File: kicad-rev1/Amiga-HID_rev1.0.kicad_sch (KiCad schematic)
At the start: 0 parts

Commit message: One Top-Level Schematic
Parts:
- added C1: 10uF, Capacitor_SMD:C_0805_2012Metric, symbol Device:C
- added C10, C9: 4.7u, Capacitor_SMD:C_0402_1005Metric, symbol Device:C
- added C11, C12, C13, C14, C15, C16, C17, C18, C2, C8: 100n, Capacitor_SMD:C_0402_1005Metric, symbol Device:C
- added C19: 10u, Capacitor_SMD:C_0805_2012Metric, symbol Device:C
- added C2, C21, C23, C4: 100nF, Capacitor_SMD:C_0402_1005Metric, symbol Device:C
- added C3: 22uF, Capacitor_SMD:C_0805_2012Metric, symbol Device:C
- added C3, C4: 15p, Capacitor_SMD:C_0402_1005Metric, symbol Device:C
- added C6, C7: 4.7u, Amiga-HID_rev1.0:C_0402_1005Metric_small_pads, symbol Device:C
- added D1, D2, D3: PMEG2010AEH, Diode_SMD:D_SOD-323, symbol Device:D_Schottky
- added F1: 500mA, Fuse:Fuse_1206_3216Metric, symbol Device:Polyfuse
- added J1: USB-A Host, Connector_USB:USB_A_Stewart_SS-52100-001_Horizontal, symbol Connector:USB_A
- added J2: JST-XH-5A, Connector_JST:JST_XH_B5B-XH-A_1x05_P2.50mm_Vertical, symbol Connector_Generic:Conn_01x05
- added J3: OLED I2C, Connector_PinHeader_2.54mm:PinHeader_1x04_P2.54mm_Vertical, symbol Connector_Generic:Conn_01x04
- added J4: Reserve 3V3+GP+GND+VSYS, Connector_PinHeader_2.54mm:PinHeader_1x05_P2.54mm_Vertical, symbol Connector_Generic:Conn_01x05
- added J5: JST-SH-3 SWD, Connector_JST:JST_SH_SM03B-SRSS-TB_1x03-1MP_P1.00mm_Horizontal, symbol Connector_Generic:Conn_01x03
- added J6: JST-SH-3 UART, Connector_JST:JST_SH_SM03B-SRSS-TB_1x03-1MP_P1.00mm_Horizontal, symbol Connector_Generic:Conn_01x03
- added L1: 3.3u, Amiga-HID_rev1.0:L_pol_2016, symbol Device:L
- added LED1: Status_Green, LED_SMD:LED_0603_1608Metric, symbol Device:LED
- added LED2: Activity_Yellow, LED_SMD:LED_0603_1608Metric, symbol Device:LED
- added R1, R9: DNF, Resistor_SMD:R_0402_1005Metric, symbol Device:R
- added R1, R2: 1k, Resistor_SMD:R_0603_1608Metric, symbol Device:R
- added R10: 0, Resistor_SMD:R_0402_1005Metric, symbol Device:R
- added R2, R4, R6: 1k, Resistor_SMD:R_0402_1005Metric, symbol Device:R
- added R5: 33, Resistor_SMD:R_0402_1005Metric, symbol Device:R
- added R7, R8: 27, Resistor_SMD:R_0402_1005Metric, symbol Device:R
- added SJ1: OLED_VCC_SEL, Jumper:SolderJumper-3_P1.3mm_Open_TrianglePad1.0x1.5mm, symbol Jumper:SolderJumper_3_Bridged12
- added SW1, SW2: SW_Push, Button_Switch_SMD:SW_Push_1P1T_NO_Vertical_Wuerth_434133025816, symbol Switch:SW_Push
- added U1: RP2350_60QFN, Amiga-HID_rev1.0:RP2350-QFN-60-1EP_7x7_P0.4mm_EP3.4x3.4mm_ThermalVias, symbol MCU_RaspberryPi_RP2350:RP2350_60QFN
- added U1: USBLC6-2SC6, Package_TO_SOT_SMD:SOT-23-6, symbol Power_Protection:USBLC6-2SC6
- added U2: AMS1117-3.3, Package_TO_SOT_SMD:SOT-223-3_TabPin2, symbol Regulator_Linear:AMS1117-3.3
- added U3: W25Q128JVS, Package_SO:SOIC-8_5.23x5.23mm_P1.27mm, symbol Memory_Flash:W25Q128JVS
- added U5: TXS0102DCUR, Package_SO:VSSOP-8_2.4x2.0mm_P0.5mm, symbol Custom:TXS0102
- added Y1: ABM8-272-T3, Crystal:Crystal_SMD_3225-4Pin_3.2x2.5mm, symbol Device:Crystal_GND24
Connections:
- new net: R7.2, U1.52 (USB_DP)
- new net: R8.2, U1.51 (USB_DM)
- new net: J3.2 (Pin_2), SJ1.1 (A)
- new net: R4.1, SW2.1
- new net: LED1.1 (K), R1.1
- new net: LED2.1 (K), R2.2
- new net: C4.1, R2.2, Y1.3
- new net: D3.1 (K), F1.1
- new net +1V1: C10.1, C11.1, C7.1, C8.1, L1.1, U1.23 (DVDD), U1.39 (DVDD), U1.50 (VREG_FB), U1.6 (DVDD)
- new net +3V3: C12.1, C13.1, C14.1, C15.1, C16.1, C17.1, C18.1, C19.1, C2.1, C21.2, C3.1, C4.1, C6.1, J4.3 (Pin_3), R1.1, R5.1, SJ1.2 (C), U1.1 (IOVDD), U1.11 (IOVDD), U1.20 (IOVDD), U1.30 (IOVDD), U1.38 (IOVDD), U1.44 (ADC_AVDD), U1.45 (IOVDD), U1.49 (VREG_VIN), U1.53 (USB_OTP_VDD), U1.54 (QSPI_IOVDD), U2.2 (VO), U3.8 (VCC), U5.1 (VCCA), U5.5 (OE)
- new net +5V_AMIGA: D2.2 (A), J2.4 (Pin_4)
- new net FLASH_SS: R1.2, R10.2, R9.2, U3.1 (~{CS})
- new net GND: C1.2, C10.2, C11.2, C12.2, C13.2, C14.2, C15.2, C16.2, C17.2, C18.2, C19.2, C2.2, C2.2, C21.1, C23.1, C3.2, C3.2, C4.2, C4.2, C6.2, C7.2, C8.2, C9.2, J1.4 (GND), J1.5 (Shield), J2.5 (Pin_5), J3.1 (Pin_1), J4.2 (Pin_2), J5.2 (Pin_2), J6.2 (Pin_2), LED1.2 (A), LED2.2 (A), R4.2, SW1.1, U1.2 (GND), U1.47 (VREG_PGND), U1.61 (GND), U2.1 (GND), U3.4 (GND), U5.4 (GND), Y1.2, Y1.4
- new net GPIO10: U1.14 (GPIO10)
- new net GPIO11: U1.15 (GPIO11)
- new net GPIO12: U1.16 (GPIO12)
- new net GPIO13: U1.17 (GPIO13)
- new net GPIO14: U1.18 (GPIO14)
- new net GPIO15: U1.19 (GPIO15)
- new net GPIO17: U1.28 (GPIO17)
- new net GPIO18: U1.29 (GPIO18)
- new net GPIO19: U1.31 (GPIO19)
- new net GPIO20: U1.32 (GPIO20)
- new net GPIO21: U1.33 (GPIO21)
- new net GPIO22: U1.34 (GPIO22)
- new net GPIO23: U1.35 (GPIO23)
- new net GPIO24: U1.36 (GPIO24)
- new net GPIO26_ADC0: U1.40 (GPIO26_ADC0)
- new net GPIO27_ADC1: U1.41 (GPIO27_ADC1)
- new net GPIO28_ADC2: U1.42 (GPIO28_ADC2)
- new net GPIO29_ADC3: U1.43 (GPIO29_ADC3)
- new net GPIO4: U1.7 (GPIO4)
- new net GPIO9: U1.13 (GPIO9)
- new net GP_RES1: J4.4 (Pin_4), U1.10 (GPIO7)
- new net GP_RES2: J4.5 (Pin_5), U1.12 (GPIO8)
- new net I2C1_SCL: J3.3 (Pin_3), U1.5 (GPIO3)
- new net I2C1_SDA: J3.4 (Pin_4), U1.4 (GPIO2)
- new net KB_CLOCK_3V3: U1.9 (GPIO6), U5.3 (A2)
- new net KB_CLOCK_5V: J2.1 (Pin_1), U5.6 (B2)
- new net KB_DATA_3V3: U1.8 (GPIO5), U5.2 (A1)
- new net KB_DATA_5V: J2.3 (Pin_3), U5.7 (B1)
- new net LED1: R1.2, U1.37 (GPIO25)
- new net LED2: R2.1, U1.27 (GPIO16)
- new net QSPI_SCLK: U1.56 (QSPI_SCLK), U3.6 (CLK)
- new net QSPI_SD0: U1.57 (QSPI_SD0), U3.5 (DI(IO0))
- new net QSPI_SD1: U1.59 (QSPI_SD1), U3.2 (DO(IO1))
- new net QSPI_SD2: U1.58 (QSPI_SD2), U3.3 (IO2)
- new net QSPI_SD3: U1.55 (QSPI_SD3), U3.7 (IO3)
- new net QSPI_SS: R10.1, R6.1, U1.60 (QSPI_SS)
- new net RUN: SW2.2, U1.26 (RUN)
- new net SWCLK: J5.1 (Pin_1), U1.24 (SWCLK)
- new net SWDIO: J5.3 (Pin_3), U1.25 (SWD)
- new net UART_RX: J6.3 (Pin_3), U1.3 (GPIO1)
- new net UART_TX: J6.1 (Pin_1), R9.1, U1.2 (GPIO0)
- new net USB_D+: J1.3 (D+), U1.1 (I/O1)
- new net USB_D-: J1.2 (D-), U1.3 (I/O2)
- new net USB_DM: R8.1, U1.4 (I/O2)
- new net USB_DP: R7.1, U1.6 (I/O1)
- new net VBUS: C23.2, D1.2 (A), F1.2, J1.1 (VBUS), U1.5 (VBUS), U5.8 (VCCB)
- new net VREG_AVDD: C9.1, R5.2, U1.46 (VREG_AVDD)
- new net VREG_LX: L1.2, U1.48 (VREG_LX)
- new net VSYS: C1.1, C2.1, D1.1 (K), D2.1 (K), D3.2 (A), J4.1 (Pin_1), SJ1.3 (B), U2.3 (VI)
- new net XIN: C3.1, U1.21 (XIN), Y1.1
- new net XOUT: R2.1, U1.22 (XOUT)
- new net ~{USB_BOOT}: R6.2, SW1.2
- no-connect marks 0 -> 21
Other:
- removed sheet MCU
- removed sheet Power
- note added: "12MHz Crystal"
- note added: "Debug-Pads Bereich A (1.0mm Pitch) - Pi Debug Probe"
- note added: "Debug-Pads Bereich B (2.54mm Pitch) - OLED + Reserve"
- note added: "Flash"
- note added: "Level Shifter TXS0102 -- 3V3 (RP2350) <-> 5V (Amiga)"
- note added: "Make sure R7 and R8 are close to RP2350"
- note added: "Signale vom/zum MCU-Sheet:"
- note added: "Status & Activity LEDs"
- note added: "USB-A Buchse (Host: Tastatur / Service: PC fuer Flash)"
- note added: "VSYS rail = 4.8 V worst-case\nKeyboard sees ~4.55 V via D3+F1 (within USB spec)"
- note removed: "Amiga-HID rev1.0 - top level. Iteration 1: Power section only. Further sheets (mcu, usb, level_shifter, connectors_debug) to be added."
- title: Amiga-HID rev1.0 - Top Level -> Amiga-HID rev1.0

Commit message: Footprints sind vollständig
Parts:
- added J7: Conn_01x06_Pin, Connector_PinHeader_1.27mm:PinHeader_1x06_P1.27mm_Vertical, symbol Connector:Conn_01x06_Pin
- C8: renamed from C6; footprint Amiga-HID_rev1.0:C_0402_1005Metric_small_pads -> Capacitor_SMD:C_0402_1005Metric
- C9: renamed from C7; footprint Amiga-HID_rev1.0:C_0402_1005Metric_small_pads -> Capacitor_SMD:C_0402_1005Metric
- L1: value 3.3u -> 2.2u; Alternate (none) -> 3.3uH: Sunlord MWSA201610H3R3MT (LCSC C408237) - same footp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; LCSC (none) -> C408232; MPN (none) -> MWSA201610H2R2MT; Manufacturer (none) -> Sunlord
- SJ1: footprint Jumper:SolderJumper-3_P1.3mm_Open_TrianglePad1.0x1.5mm -> Jumper:SolderJumper-3_P1.3mm_Open_Pad1.0x1.5mm
- U5: footprint Package_SO:VSSOP-8_2.4x2.0mm_P0.5mm -> Package_SO:VSSOP-8_2.3x2mm_P0.5mm
- Y1: value ABM8-272-T3 -> 12MHz_3225_8pF
- renumbered C8 to C10, C9 to C11, C10 to C12, C11 to C13, C19 to C14, C12 to C15, C13 to C16, C14 to C17, C15 to C18, C16 to C19, C17 to C20, C18 to C22, C3 to C5, C4 to C6, C2 to C7, R7 to R10, R8 to R11, R9 to R3, R10 to R4, R1 to R5, R2 to R6, R4 to R7, R5 to R8, R6 to R9, U1 to U4
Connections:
- net GND: now also J7.2 (Pin_2), J7.5 (Pin_5)
- net SWCLK: now also J7.1 (Pin_1)
- net SWDIO: now also J7.3 (Pin_3)
- net UART_RX: now also J7.6 (Pin_6)
- net UART_TX: now also J7.4 (Pin_4)

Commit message: korrekte USB-A Buchse
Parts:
- J1: footprint Connector_USB:USB_A_Stewart_SS-52100-001_Horizontal -> Amiga-HID_rev1.0:USB_A_Receptacle_Edge_C42614
- J5: footprint Connector_JST:JST_SH_SM03B-SRSS-TB_1x03-1MP_P1.00mm_Horizontal -> Connector_JST:JST_SH_BM03B-SRSS-TB_1x03-1MP_P1.00mm_Vertical
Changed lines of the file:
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@@
 			)
 		)
-		(property "Footprint" "Connector_USB:USB_A_Stewart_SS-52100-001_Horizontal"
+		(property "Footprint" "Amiga-HID_rev1.0:USB_A_Receptacle_Edge_C42614"
 			(at 24.13 83.82 0)
 			(effects
@@
 			)
 		)
-		(property "Datasheet" ""
+		(property "Datasheet" "~"
 			(at 24.13 83.82 0)
 			(effects
@@
 			)
 		)
-		(property "Description" ""
+		(property "Description" "USB Type A connector"
 			(at 24.13 83.82 0)
 			(effects
@@
 	)
 	(symbol
+		(lib_name "Conn_01x03_1")
 		(lib_id "Connector_Generic:Conn_01x03")
 		(at 210.82 250.19 0)
@@
 			)
 		)
-		(property "Footprint" "Connector_JST:JST_SH_SM03B-SRSS-TB_1x03-1MP_P1.00mm_Horizontal"
+		(property "Footprint" "Connector_JST:JST_SH_BM03B-SRSS-TB_1x03-1MP_P1.00mm_Vertical"
 			(at 210.82 250.19 0)
 			(effects
@@
 			)
 		)
-		(property "Datasheet" ""
+		(property "Datasheet" "~"
 			(at 210.82 250.19 0)
 			(effects
@@
 			)
 		)
-		(property "Description" ""
+		(property "Description" "Generic connector, single row, 01x03, script generated (kicad-library-utils/schlib/autogen/connector/)"
 			(at 210.82 250.19 0)
 			(effects

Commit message: alle 3d modelle implementiert
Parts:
- J5: footprint Connector_JST:JST_SH_BM03B-SRSS-TB_1x03-1MP_P1.00mm_Vertical -> Connector_JST:JST_SH_SM03B-SRSS-TB_1x03-1MP_P1.00mm_Horizontal
- SW1, SW2: footprint Button_Switch_SMD:SW_Push_1P1T_NO_Vertical_Wuerth_434133025816 -> Amiga-HID_rev1.0:SW_SMD_Tact_4x3_4P_C139797
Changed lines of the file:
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@@
 			)
 		)
-		(property "Footprint" "Connector_JST:JST_SH_BM03B-SRSS-TB_1x03-1MP_P1.00mm_Vertical"
+		(property "Footprint" "Connector_JST:JST_SH_SM03B-SRSS-TB_1x03-1MP_P1.00mm_Horizontal"
 			(at 210.82 250.19 0)
 			(effects
@@
 			)
 		)
-		(property "Footprint" "Button_Switch_SMD:SW_Push_1P1T_NO_Vertical_Wuerth_434133025816"
+		(property "Footprint" "Amiga-HID_rev1.0:SW_SMD_Tact_4x3_4P_C139797"
 			(at 153.67 163.83 0)
 			(effects
@@
 			)
 		)
-		(property "Footprint" "Button_Switch_SMD:SW_Push_1P1T_NO_Vertical_Wuerth_434133025816"
+		(property "Footprint" "Amiga-HID_rev1.0:SW_SMD_Tact_4x3_4P_C139797"
 			(at 143.51 134.62 0)
 			(effects

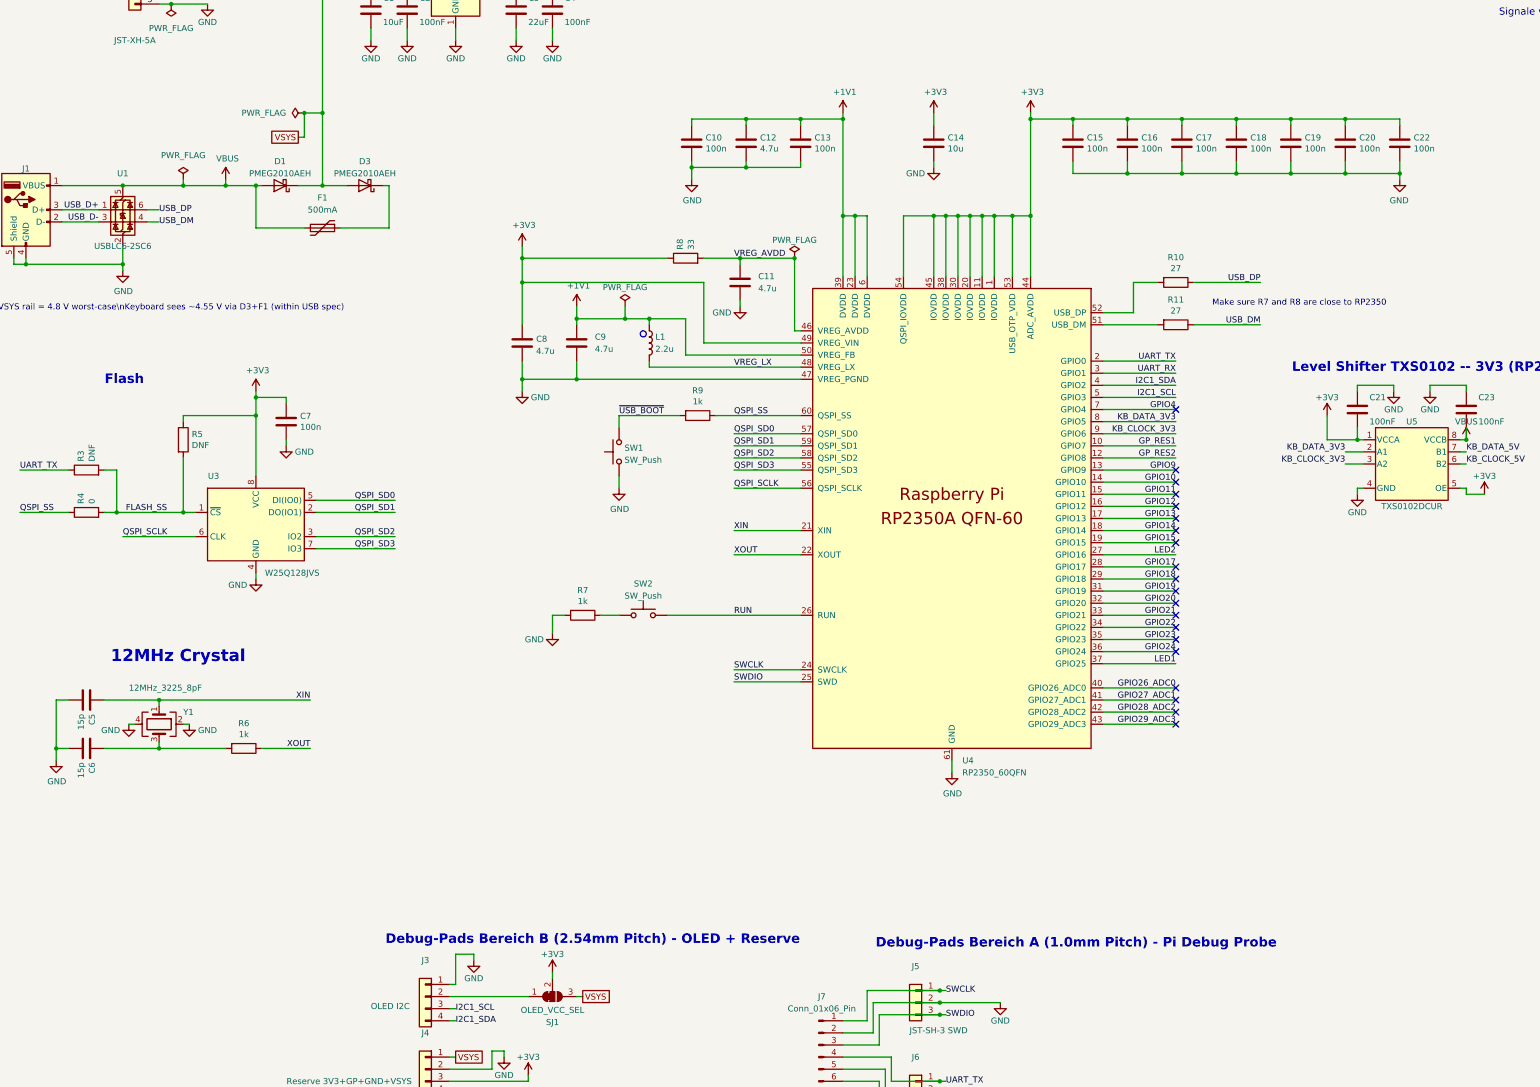
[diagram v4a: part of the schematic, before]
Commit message: aufteilung Bauteile Vorder und Rückseite
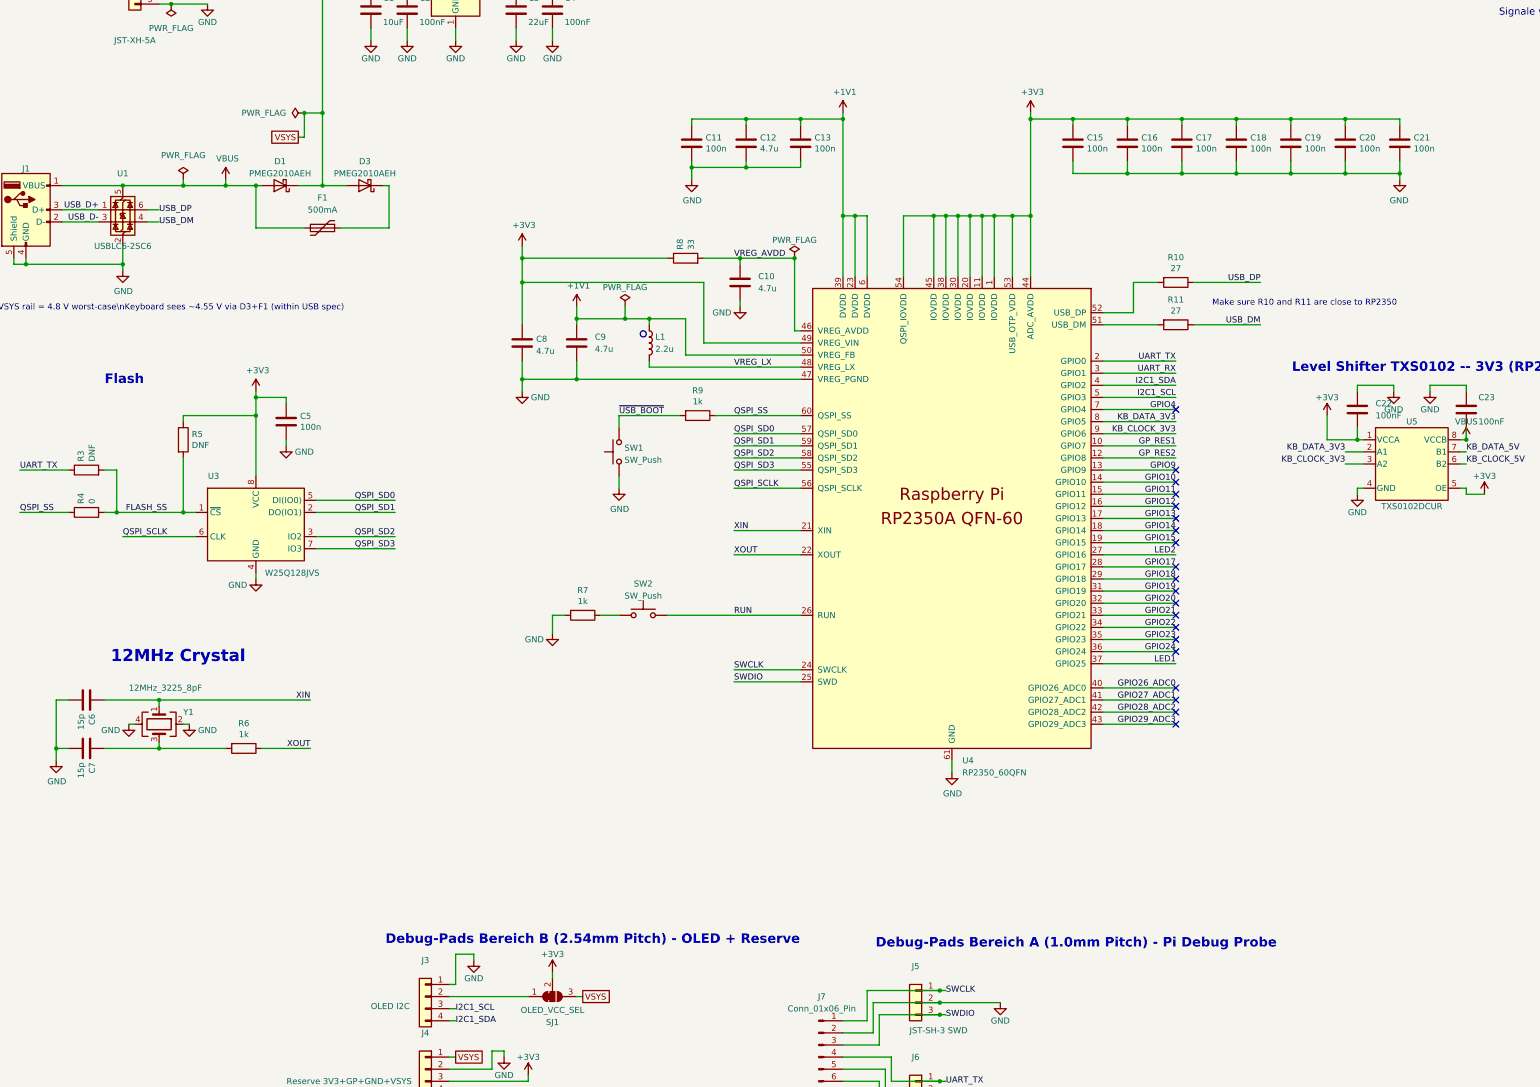
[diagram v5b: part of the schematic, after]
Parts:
- removed C14: 10u, Capacitor_SMD:C_0805_2012Metric, symbol Device:C
- U3: footprint Package_SO:SOIC-8_5.23x5.23mm_P1.27mm -> Amiga-HID_rev1.0:SOIC-8_5.3x5.3mm_P1.27mm; LCSC (none) -> C113767
- renumbered C11 to C10, C10 to C11, C22 to C21, C21 to C22, C7 to C5, C5 to C6, C6 to C7
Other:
- note added: "Make sure R10 and R11 are close to RP2350"
- note removed: "Make sure R7 and R8 are close to RP2350"
